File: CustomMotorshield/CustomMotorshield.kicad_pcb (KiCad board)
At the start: 2 copper layers, 40.5 x 56 mm, 7 parts, among them J1 Conn_01x20, J2 Conn_01x20

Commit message: Updated PCB !
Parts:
- added D1: LED, LED_SMD:LED_2512_6332Metric, F.Cu at (81.5, 81.0)
- added D2: LED, LED_SMD:LED_2512_6332Metric, F.Cu at (81.5, 69.5)
- added D3: LED, LED_SMD:LED_2512_6332Metric, F.Cu at (81.6, 58.0)
- added D4: LED, LED_SMD:LED_2512_6332Metric, F.Cu at (81.6, 46.5)
- added D5: LED, LED_SMD:LED_2512_6332Metric, F.Cu at (76.7, 35.5)
- added D6: LED, LED_SMD:LED_2512_6332Metric, F.Cu at (84.9, 35.5)
- added D7: LED, LED_SMD:LED_2512_6332Metric, F.Cu at (93.0, 35.5)
- added R1: R, Resistor_SMD:R_1206_3216Metric_Pad1.30x1.75mm_HandSolder, F.Cu at (81.5, 85.5)
- added R2: R, Resistor_SMD:R_1206_3216Metric_Pad1.30x1.75mm_HandSolder, F.Cu at (81.5, 74.0)
- added R3: R, Resistor_SMD:R_1206_3216Metric_Pad1.30x1.75mm_HandSolder, F.Cu at (81.5, 62.4)
- added R4: R, Resistor_SMD:R_1206_3216Metric_Pad1.30x1.75mm_HandSolder, F.Cu at (81.5, 50.8)
- added R5: R, Resistor_SMD:R_1206_3216Metric_Pad1.30x1.75mm_HandSolder, F.Cu at (76.6, 40.5)
- added R6: R, Resistor_SMD:R_1206_3216Metric_Pad1.30x1.75mm_HandSolder, F.Cu at (85.0, 40.4)
- added R7: R, Resistor_SMD:R_1206_3216Metric_Pad1.30x1.75mm_HandSolder, F.Cu at (93.0, 40.3)
- moved Motor4 6.52 mm to (73.5, 46.0)
- moved CameraConnector1 6.18 mm to (94.0, 79.9)
- moved Motor3 6.10 mm to (73.5, 57.5)
- moved Motor2 5.70 mm to (73.5, 69.0)
- moved Motor1 5.32 mm to (73.5, 80.5)
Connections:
- J2 pad 12: unconnected-(J2-Pin_12-Pad12) -> IO35
- J2 pad 13: unconnected-(J2-Pin_13-Pad13) -> IO48
- J2 pad 14: unconnected-(J2-Pin_14-Pad14) -> IO34
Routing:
- net GND: track 81.8 -> 149.1 mm
- net IO34: track 0.00 -> 55.3 mm
- net IO48: track 0.00 -> 45.5 mm
- net IO35: track 0.00 -> 35.2 mm
- net 5V: track 61.8 -> 45.7 mm
- net D0: track 25.3 -> 12.8 mm
- net D2: track 15.3 -> 27.3 mm
- net IO21: track 10.5 -> 18.2 mm
- net IO26: track 16.7 -> 23.3 mm
- net IO47: track 26.2 -> 32.3 mm
- net IO33: track 35.7 -> 41.3 mm
- net D1: track 12.8 -> 18.2 mm
- net Net-(D1-K): track 0.00 -> 5.07 mm
- net Net-(D2-K): track 0.00 -> 5.06 mm
- net Net-(D5-K): track 0.00 -> 5.03 mm
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
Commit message: Latest PCB !
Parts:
- D1, D2, D3, D4, D5, D6, D7: footprint LED_SMD:LED_2512_6332Metric -> LED_SMD:LED_0603_1608Metric_Pad1.05x0.95mm_HandSolder
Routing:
- net GND: track 149.1 -> 1.64 mm, vias 0 -> 7
- net 5V: track 45.7 -> 52.1 mm
- net IO47: track 32.3 -> 30.3 mm
- net IO33: track 41.3 -> 39.3 mm
- net IO26: track 23.3 -> 21.3 mm
- net IO21: track 18.2 -> 16.2 mm
- net IO35: track 35.2 -> 34.8 mm, vias 0 -> 1
- net IO34: track 55.3 -> 55.0 mm, vias 0 -> 1
- net IO48: track 45.5 -> 45.2 mm, vias 0 -> 1
- added copper zone on B.Cu, net GND
- added copper zone on F.Cu, net GND

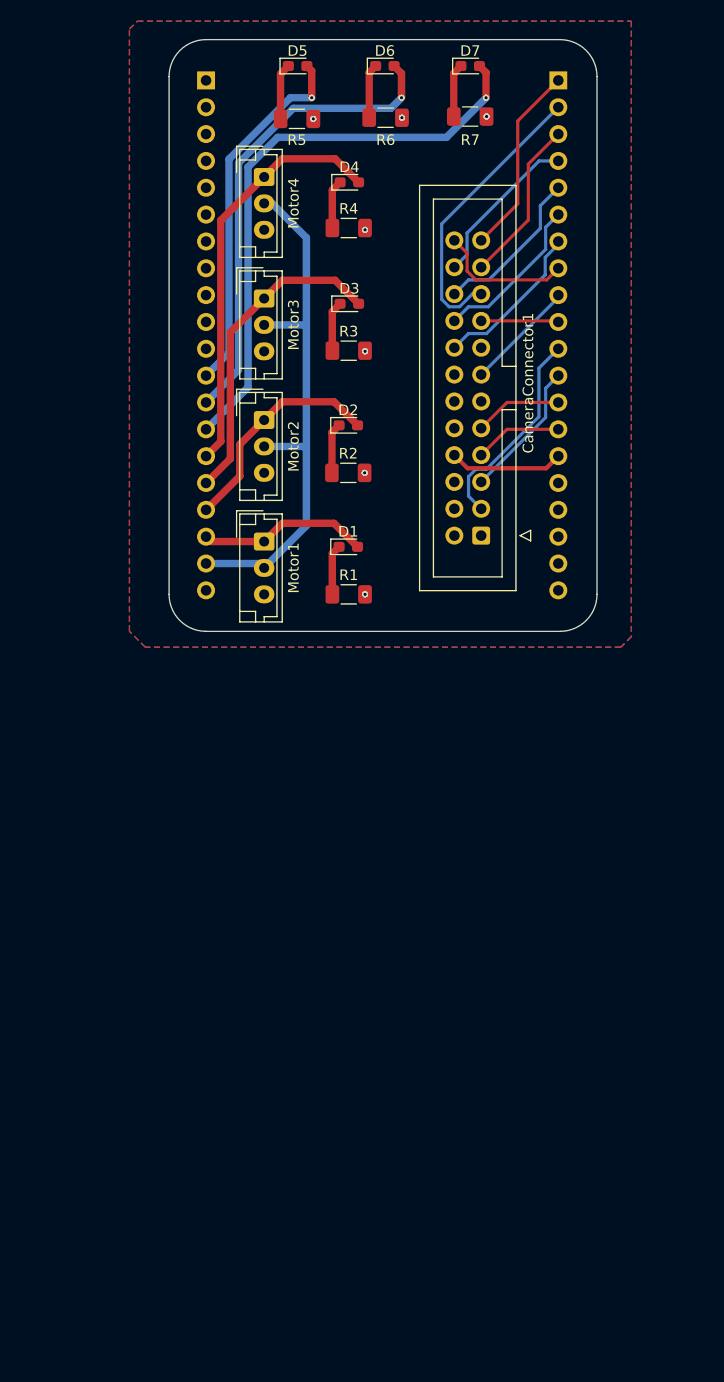
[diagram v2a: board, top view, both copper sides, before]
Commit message: new PCB with VR
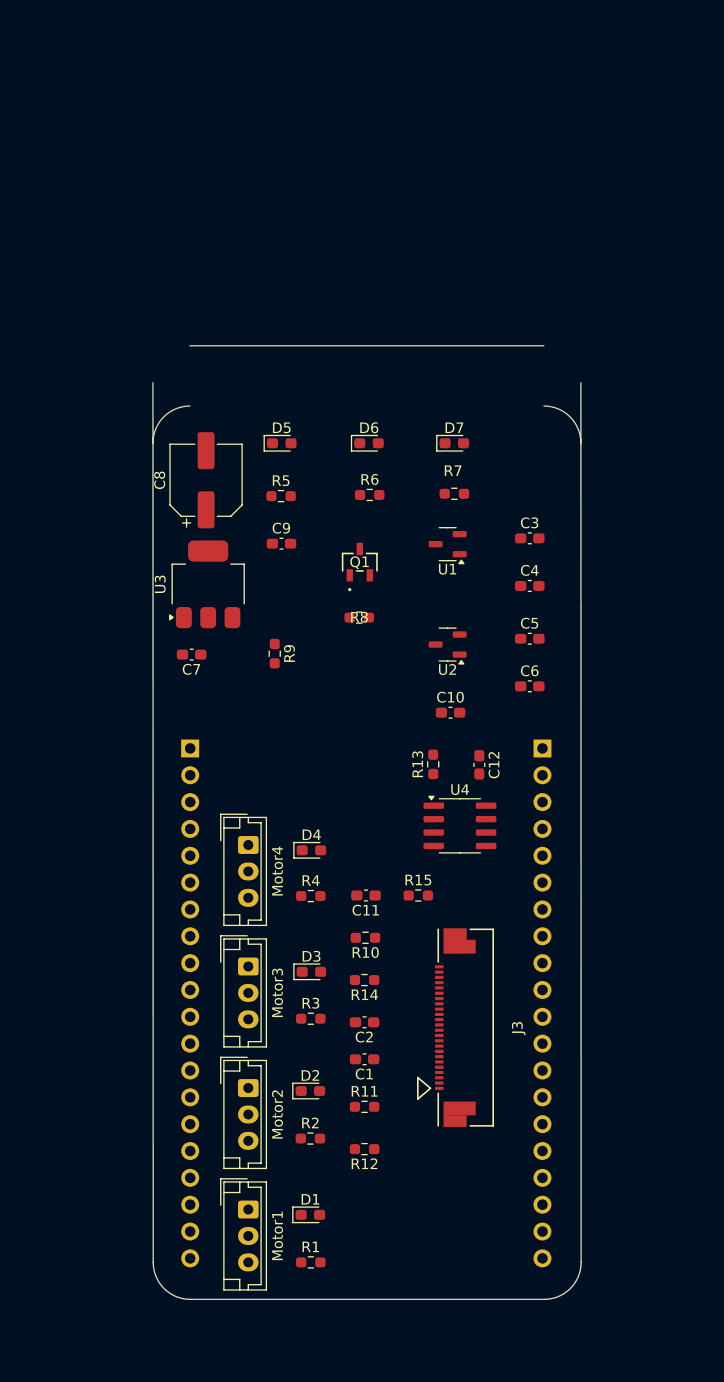
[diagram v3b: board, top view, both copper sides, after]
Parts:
- removed CameraConnector1: Conn_02x12_Top_Bottom, Connector_IDC:IDC-Header_2x12_P2.54mm_Vertical
- added C1: 15pF, Capacitor_SMD:C_0603_1608Metric_Pad1.08x0.95mm_HandSolder, F.Cu at (83.0, 129.5)
- added C10: 10uF, Capacitor_SMD:C_0603_1608Metric_Pad1.08x0.95mm_HandSolder, F.Cu at (91.1, 96.7)
- added C11: 0.1uF, Capacitor_SMD:C_0603_1608Metric_Pad1.08x0.95mm_HandSolder, F.Cu at (83.1, 114.0)
- added C12: 1uF, Capacitor_SMD:C_0603_1608Metric_Pad1.08x0.95mm_HandSolder, F.Cu at (93.9, 101.6)
- added C2: 0.1uF, Capacitor_SMD:C_0603_1608Metric_Pad1.08x0.95mm_HandSolder, F.Cu at (83.0, 126.0)
- added C3: 10uF, Capacitor_SMD:C_0603_1608Metric_Pad1.08x0.95mm_HandSolder, F.Cu at (98.6, 80.2)
- added C4: 0.1uF, Capacitor_SMD:C_0603_1608Metric_Pad1.08x0.95mm_HandSolder, F.Cu at (98.6, 84.7)
- added C5: 10uF, Capacitor_SMD:C_0603_1608Metric_Pad1.08x0.95mm_HandSolder, F.Cu at (98.6, 89.7)
- added C6: 0.1uF, Capacitor_SMD:C_0603_1608Metric_Pad1.08x0.95mm_HandSolder, F.Cu at (98.6, 94.2)
- added C7: 10uF, Capacitor_SMD:C_0603_1608Metric_Pad1.08x0.95mm_HandSolder, F.Cu at (66.6, 91.2)
- added C8: 100uF, Capacitor_SMD:CP_Elec_6.3x5.4, F.Cu at (68.0, 74.7)
- added C9: 10uF, Capacitor_SMD:C_0603_1608Metric_Pad1.08x0.95mm_HandSolder, F.Cu at (75.1, 80.7)
- added J3: 524352471, CON_524352471_MOL:CON_524352471_MOL, F.Cu at (92.6, 126.5)
- added Q1: BSS84PH6327XTSA2, SOT23_BSS84_INF-L:SOT23_BSS84_INF-M, F.Cu at (82.5, 82.5)
- added R10: 4.7K, Resistor_SMD:R_0603_1608Metric_Pad0.98x0.95mm_HandSolder, F.Cu at (83.1, 118.0)
- added R11: 4.7K, Resistor_SMD:R_0603_1608Metric_Pad0.98x0.95mm_HandSolder, F.Cu at (83.0, 134.0)
- added R12: 4.7K, Resistor_SMD:R_0603_1608Metric_Pad0.98x0.95mm_HandSolder, F.Cu at (83.0, 138.0)
- added R13: 10K, Resistor_SMD:R_0603_1608Metric_Pad0.98x0.95mm_HandSolder, F.Cu at (89.5, 101.6)
- added R14: 1K, Resistor_SMD:R_0603_1608Metric_Pad0.98x0.95mm_HandSolder, F.Cu at (83.0, 122.0)
- added R15: 10K, Resistor_SMD:R_0603_1608Metric_Pad0.98x0.95mm_HandSolder, F.Cu at (88.1, 114.0)
- added R8: 10k, Resistor_SMD:R_0603_1608Metric_Pad0.98x0.95mm_HandSolder, F.Cu at (82.5, 87.7)
- added R9: 1k, Resistor_SMD:R_0603_1608Metric_Pad0.98x0.95mm_HandSolder, F.Cu at (74.5, 91.1)
- added U1: XC6206P282MR, Package_TO_SOT_SMD:SOT-23-3, F.Cu at (90.9, 80.8)
- added U2: XC6206P122MR, Package_TO_SOT_SMD:SOT-23-3, F.Cu at (90.9, 90.2)
- added U3: AMS1117-3.3, Package_TO_SOT_SMD:SOT-223-3_TabPin2, F.Cu at (68.2, 84.5)
- added U4: ESP-PSRAM32, Package_SO:SOIC-8_3.9x4.9mm_P1.27mm, F.Cu at (92.0, 107.4)
- R1, R2, R3, R4, R5, R6: value R -> 68; footprint Resistor_SMD:R_1206_3216Metric_Pad1.30x1.75mm_HandSolder -> Resistor_SMD:R_0603_1608Metric_Pad0.98x0.95mm_HandSolder
- R7: value R -> 5.1; footprint Resistor_SMD:R_1206_3216Metric_Pad1.30x1.75mm_HandSolder -> Resistor_SMD:R_0603_1608Metric_Pad0.98x0.95mm_HandSolder
- moved D1 63.3 mm to (77.9, 144.2)
- moved D3 63.3 mm to (78.0, 121.2)
- moved D4 63.3 mm to (78.0, 109.7)
- moved R1 63.3 mm to (77.9, 148.7)
- moved R3 63.3 mm to (77.9, 125.7)
- moved R4 63.3 mm to (77.9, 114.0)
- moved J1 63.2 mm to (99.8, 100.1)
- moved J2 63.2 mm to (66.5, 100.1)
- moved Motor1 63.2 mm to (72.0, 143.7)
- moved Motor2 63.2 mm to (72.0, 132.2)
- moved Motor3 63.2 mm to (72.0, 120.7)
- moved Motor4 63.2 mm to (72.0, 109.2)
- moved D2 63.1 mm to (77.9, 132.5)
- moved R2 63.1 mm to (77.9, 137.0)
- moved D5 35.7 mm to (75.2, 71.2)
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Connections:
- J1 pad 1: D1 -> CSI_D1
- J1 pad 10: PCLK -> CSI_PCLK
- J1 pad 11: SIOD -> TWI_SDA
- J1 pad 12: SIOC -> TWI_SCK
- J1 pad 13: HREF -> CSI_VSYNC
- J1 pad 14: VSYNC -> PSRAM_CLK
- J1 pad 15: PWDN -> unconnected-(J1-Pin_15-Pad15)
- J1 pad 16: unconnected-(J1-Pin_16-Pad16) -> IO16
- J1 pad 19: 3.3V -> 3V3
- J1 pad 2: D2 -> CSI_D2
- J1 pad 3: D3 -> CSI_D3
- J1 pad 4: D4 -> CSI_D4
- J1 pad 5: D5 -> CSI_D5
- J1 pad 6: D6 -> CSI_D6
- J1 pad 7: D7 -> CSI_D7
- J1 pad 8: D0 -> CSI_D0
- J1 pad 9: XCLK -> CSI_MCLK
- J2 pad 10: unconnected-(J2-Pin_10-Pad10) -> SD0
- J2 pad 11: unconnected-(J2-Pin_11-Pad11) -> CAM_PWR
- J2 pad 7: unconnected-(J2-Pin_7-Pad7) -> SD3
- J2 pad 8: unconnected-(J2-Pin_8-Pad8) -> SD2
- J2 pad 9: unconnected-(J2-Pin_9-Pad9) -> SD1
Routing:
- net IO34: track 55.0 -> 0.00 mm, vias 1 -> 0
- net 5V: track 52.1 -> 0.00 mm
- net IO48: track 45.2 -> 0.00 mm, vias 1 -> 0
- net IO33: track 39.3 -> 0.00 mm
- net IO35: track 34.8 -> 0.00 mm, vias 1 -> 0
- net IO47: track 30.3 -> 0.00 mm
- net D2: track 27.3 -> 0.00 mm
- net IO26: track 21.3 -> 0.00 mm
- net SIOD: track 19.7 -> 0.00 mm
- net D1: track 18.2 -> 0.00 mm
- net IO21: track 16.2 -> 0.00 mm
- net D3: track 15.6 -> 0.00 mm
- net D5: track 15.3 -> 0.00 mm
- net D6: track 15.2 -> 0.00 mm
- net D4: track 15.2 -> 0.00 mm
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- removed copper zone on B.Cu, net GND
- removed copper zone on F.Cu, net GND
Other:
- board size 40.5 x 56 mm -> 40.5 x 90.2 mm

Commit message: pcb :)
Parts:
- added J4: Screw_Terminal_01x03, TerminalBlock:TerminalBlock_Altech_AK300-3_P5.00mm, F.Cu at (83.5, 146.5)
- U1: value XC6206P282MR -> XC6206PxxxMR
- U2: value XC6206P122MR -> XC6206PxxxMR
- moved R12 24.0 mm to (83.0, 114.0)
- moved R11 16.0 mm to (83.0, 118.0), turned to 180 degrees
- moved R10 8.50 mm to (83.0, 126.5)
- moved C1 8.50 mm to (83.0, 138.0)
- moved C2 8.50 mm to (83.0, 134.5)
- moved R14 8.50 mm to (83.0, 130.5)
- moved C11 8.00 mm to (83.0, 122.0)
- turned D1 to 180 degrees
- turned D2 to 180 degrees
- turned D3 to 180 degrees
- turned D4 to 180 degrees
- turned R1 to 180 degrees
- turned R2 to 180 degrees
- turned R3 to 180 degrees
- turned R4 to 180 degrees
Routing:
- net 3V3: track 0.00 -> 155.3 mm, vias 0 -> 7
- net IO48: track 0.00 -> 115.7 mm
- net 5V: track 0.00 -> 94.7 mm, vias 0 -> 1
- net IO34: track 0.00 -> 92.2 mm
- net IO35: track 0.00 -> 64.9 mm, vias 0 -> 1
- net TWI_SDA: track 0.00 -> 64.0 mm, vias 0 -> 1
- net GND: track 0.00 -> 58.5 mm, vias 0 -> 39
- net CSI_D2: track 0.00 -> 56.7 mm
- net CSI_D5: track 0.00 -> 54.6 mm
- net CSI_2.8V: track 0.00 -> 54.4 mm, vias 0 -> 2
- net IO16: track 0.00 -> 52.4 mm
- net CSI_D1: track 0.00 -> 50.4 mm, vias 0 -> 1
- net CSI_1.2V: track 0.00 -> 48.2 mm, vias 0 -> 2
- net SD1: track 0.00 -> 48.0 mm, vias 0 -> 3
- net IO33: track 0.00 -> 47.5 mm, vias 0 -> 2
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- added copper zone on B.Cu, net GND
- added copper zone on F.Cu, net GND
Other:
- board size 40.5 x 90.2 mm -> 51 x 85.1 mm
